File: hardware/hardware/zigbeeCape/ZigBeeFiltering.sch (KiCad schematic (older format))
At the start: 13 parts

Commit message: Finished Zigbee circuitry
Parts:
- added AE?: Antenna, symbol Device:Antenna
- added C? (x2): 1.1pF, symbol Device:C
- added C? (x2): 12pF, symbol Device:C
- added C?: 1pF, symbol Device:C
- added C? (x3): DNM, symbol Device:C
- added C?: 100pF, symbol Device:C
- added C?: 5.6pF, symbol Device:C
- added L?: 15nH, symbol Device:L
- added L? (x2): 2.4nH, symbol Device:L
- added L? (x2): 2nH, symbol Device:L
- added L?: 3.3nH, symbol Device:L
- added L?: DNM, symbol Device:L
- added R? (x2): DNM/0?, symbol Device:R
- added U?: 2.4GHz_Filter, symbol Zigbee:2.4GHz_Filter
- added U?: SMA_Antenna, symbol Zigbee:SMA_Antenna
- C? (x2): value C -> 3pF
- C? (x2): value C -> 100pF
- C?: value C -> 2.7pF
- C?: value C -> 5.6pF
- C?: value C -> 1.2pF
- L? (x2): value L -> 3.9nH
- L? (x2): value L -> 10nH
- L?: value L -> 7.5nH
- L?: value L -> 22nH
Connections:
- net GND: now also C?.1, C?.2, C?.2, C?.2, C?.2, L?.2, U?.2, U?.2 (GND), U?.3, U?.4, U?.4 (GND), U?.5
- net RX_TX: now also C?.2, L?.1
- net SUB-1_GHz_RF_N renamed SUB-1_GHZ_RF_N
- net SUB-1_GHz_RF_Out: no longer names the net of C?.2
- net SUB-1_GHz_RF_Out: now also R?.2
- net SUB-1_GHz_RF_P renamed SUB-1_GHZ_RF_P
- new net: C?.2, L?.1, L?.2
- new net: C?.1, L?.1, L?.2
- new net: C?.1, C?.1, L?.2
- new net: C?.2, U?.1 (IN)
- new net: R?.1, U?.3 (OUT)
- new net: C?.1, U?.1 (INPUT)
- new net: C?.2, C?.2, R?.1, R?.2
- new net: C?.1, L?.1
- new net: C?.1, C?.1, L?.1, L?.2
- new net: AE?.1 (A), C?.2
- new net 2_4_GHZ_RF_N: C?.1, L?.1, L?.2
- new net 2_4_GHZ_RF_P: C?.1, L?.1, L?.2
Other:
- note added: "Above 3 caps are changed due to lack of FL3"
- note added: "Check if caps are needed"
- note added: "Do we need to choose?"
- note added: "Last 2 caps and inductor are for Antenna matching\n"
- note added: "Should we include P11 and P12?"
- note added: "Will this simplify debugging?"
- moved on the sheet: C?, L?

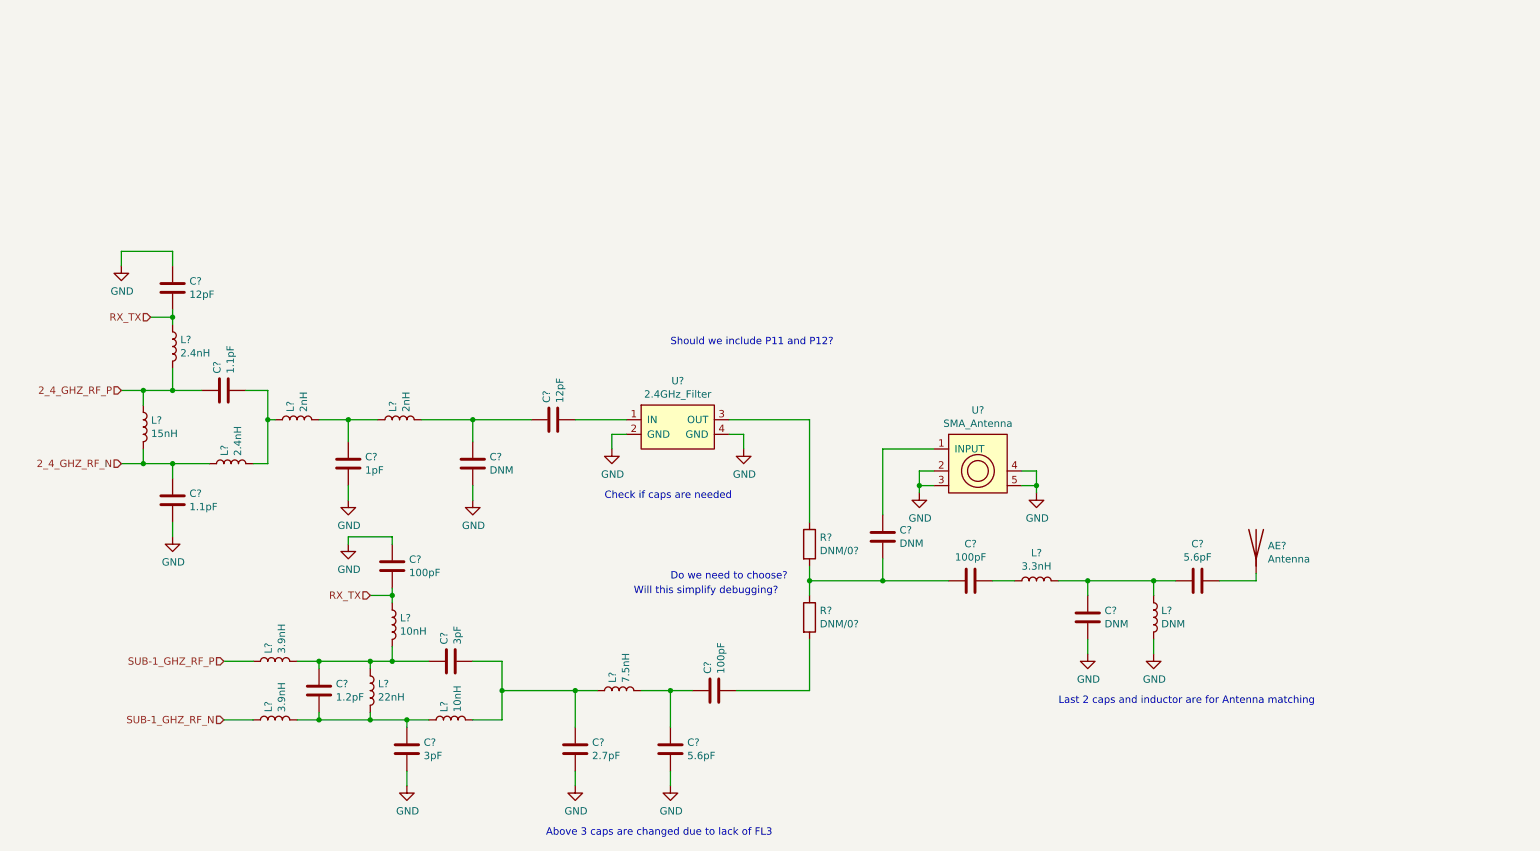
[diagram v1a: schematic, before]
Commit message: Assigned Pin types, cleaned stuff up, Fixed most errors from the DRC (questions on the last few)
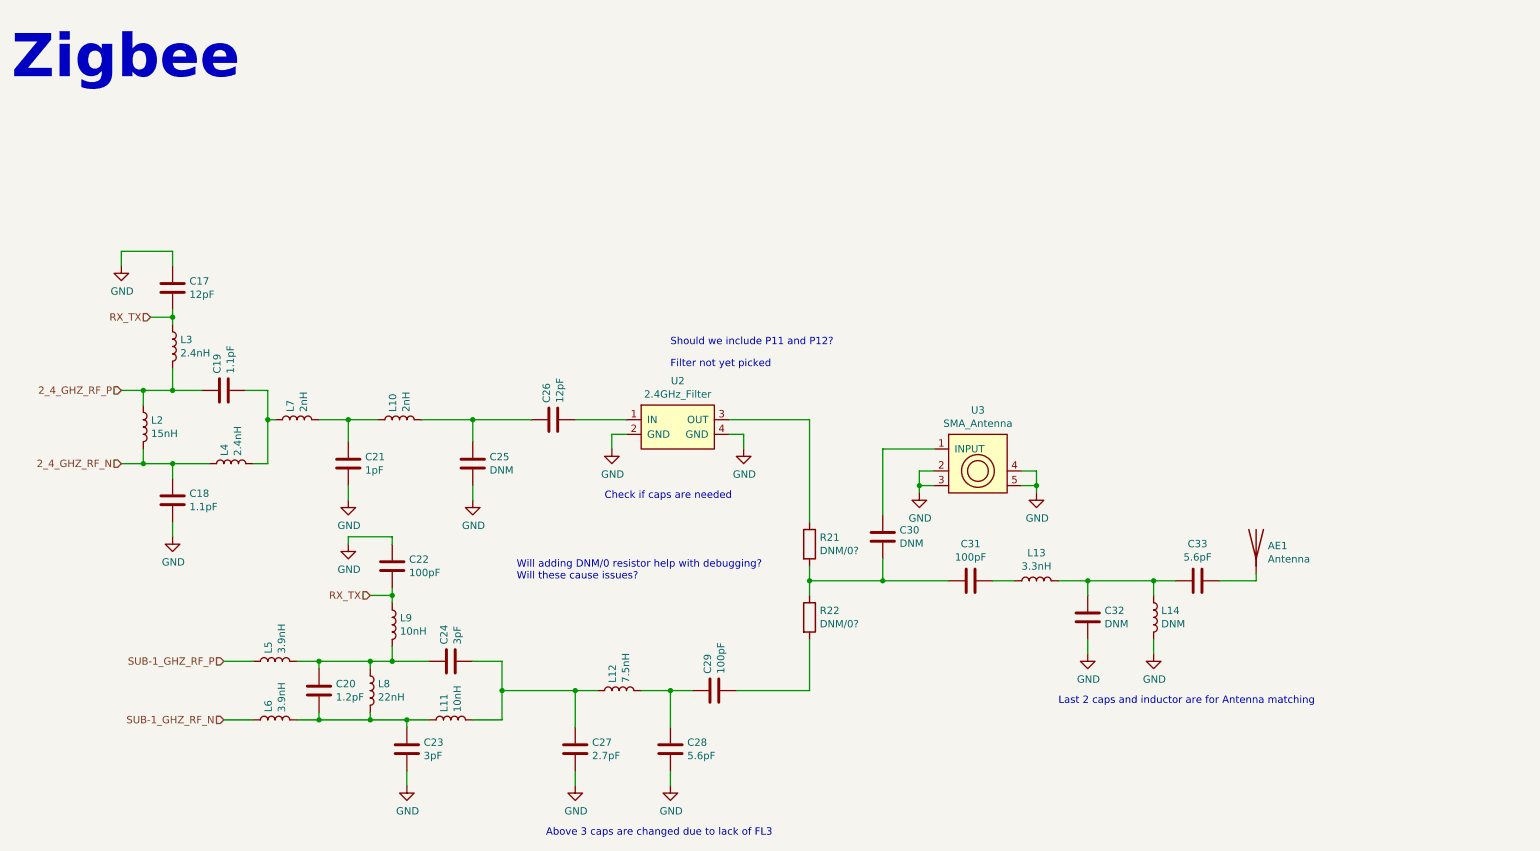
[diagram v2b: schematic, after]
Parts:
- gave numbers to parts that had none: 35
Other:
- note added: "Filter not yet picked"
- note added: "Will adding DNM/0 resistor help with debugging?\nWill these cause issues?"
- note added: "Zigbee"
- note removed: "Do we need to choose?"
- note removed: "Will this simplify debugging?"

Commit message: Added FL3 2.4ghz filter DPX252690DT-5032B1
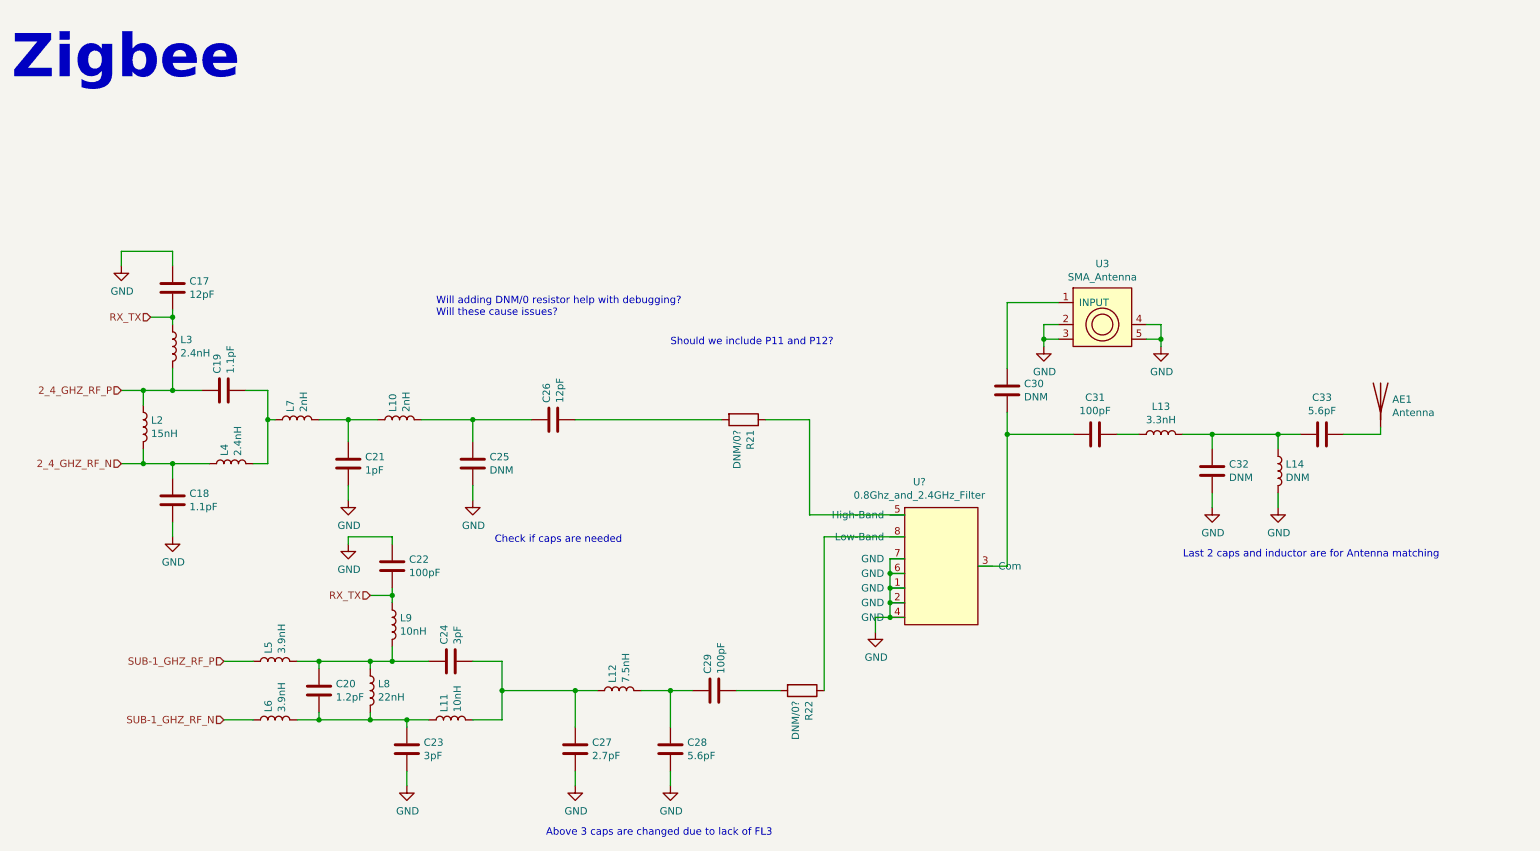
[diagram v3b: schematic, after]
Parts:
- removed U2: 2.4GHz_Filter, symbol Zigbee:2.4GHz_Filter
- added U?: 0.8Ghz_and_2.4GHz_Filter, symbol Zigbee:0.8Ghz_and_2.4GHz_Filter
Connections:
- net GND: now also U?.1 (GND), U?.2 (GND), U?.4 (GND), U?.6 (GND), U?.7 (GND)
- net at C26.2: now also R21.2
- net at R21.1: now also U?.5 (High-Band)
- net at C30.2, C31.2: now also U?.3 (Com); no longer R21.2, R22.1
- new net: R22.1, U?.8 (Low-Band)
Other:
- note removed: "Filter not yet picked"
- moved on the sheet: AE1, C30, C31, C32, C33, L13, L14, R21, R22, U3

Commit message: Fixed a few little things
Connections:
- net GND: no longer U?.1 (GND), U?.6 (GND)
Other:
- note added: "Check FL3 replacement and change parts acorrdingly"
- note added: "Remove R21 and R22"
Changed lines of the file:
@@
 	6750 4250 6650 4250
-Wire Wire Line
-	6650 4250 6650 4350
-Wire Wire Line
-	6650 4350 6750 4350
-Wire Wire Line
-	6750 4450 6650 4450
 Wire Wire Line
 	6650 4550 6750 4550
 Wire Wire Line
 	6750 4650 6650 4650
-Wire Wire Line
-	6650 4350 6650 4450
-Connection ~ 6650 4350
-Connection ~ 6650 4450
-Wire Wire Line
-	6650 4450 6650 4550
 Connection ~ 6650 4550
 Wire Wire Line
@@
 	7450 4300 7250 4300
 Connection ~ 7450 3400
+Text Notes 5450 4300 0    39   ~ 0
+Remove R21 and R22
+Text Notes 5950 5700 0    39   ~ 0
+Check FL3 replacement and change parts acorrdingly
+Wire Wire Line
+	6650 4250 6650 4550
 $EndSCHEMATC

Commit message: Fixing Git issue
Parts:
- removed R21, R22: DNM/0?, symbol Device:R
- C27: value 2.7pF -> DNM
- C28: value 5.6pF -> 3.6pF
- L12: value 7.5nH -> 9.1nH
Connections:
- net GND: now also U?.1 (GND), U?.6 (GND)
- net at C26.2: now also U?.5 (High-Band)
- net at C29.2: now also U?.8 (Low-Band)
- net at C30.2, C31.2: no longer U?.3 (Com)
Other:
- note removed: "Above 3 caps are changed due to lack of FL3"
- note removed: "Check FL3 replacement and change parts acorrdingly"
- note removed: "Check if caps are needed"
- note removed: "Remove R21 and R22"
- note removed: "Will adding DNM/0 resistor help with debugging?\nWill these cause issues?"
- moved on the sheet: AE1, C17, C18, C19, C20, C21, C22, C23, C24, C25, C26, C27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

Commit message: Started BOM
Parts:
- gave numbers to parts that had none: 1
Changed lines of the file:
@@
 Zigbee
 $Comp
-L Zigbee:0.8Ghz_and_2.4GHz_Filter U?
+L Zigbee:0.8Ghz_and_2.4GHz_Filter U2
 U 1 1 6091DA9B
 P 6300 4150
-F 0 "U?" H 6150 4625 50  0000 C CNN
+F 0 "U2" H 6150 4625 50  0000 C CNN
 F 1 "0.8Ghz_and_2.4GHz_Filter" H 6150 4534 50  0000 C CNN
 F 2 "" H 6200 4150 50  0001 C CNN

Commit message: Added excell file to document deviations from CC1352R1 footprint size. Started assigning Footprints for Zigbee cape
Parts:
- AE1: footprint (none) -> Connector_Coaxial:SMA_Amphenol_132134-16_Vertical
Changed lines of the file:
@@
 F 0 "AE1" H 9780 3989 50  0000 L CNN
 F 1 "Antenna" H 9780 3898 50  0000 L CNN
-F 2 "" H 9700 4000 50  0001 C CNN
+F 2 "Connector_Coaxial:SMA_Amphenol_132134-16_Vertical" H 9700 4000 50  0001 C CNN
 F 3 "~" H 9700 4000 50  0001 C CNN
 	1    9700 4000

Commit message: Added items to BOM. Added footprints to GIT. Finished Capacitor footprint association. Finished LED footprint association.
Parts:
- C17, C18, C19, C20, C21, C22, C23, C24, C25, C26, C27, C28, C29, C30, C31, C32, C33: footprint (none) -> Capacitor_SMD:C_0603_1608Metric_Pad1.08x0.95mm_HandSolder
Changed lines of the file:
@@
 F 0 "C24" H 3515 4946 50  0000 L CNN
 F 1 "3pF" H 3515 4855 50  0000 L CNN
-F 2 "" H 3438 4750 50  0001 C CNN
+F 2 "Capacitor_SMD:C_0603_1608Metric_Pad1.08x0.95mm_HandSolder" H 3438 4750 50  0001 C CNN
 F 3 "~" H 3400 4900 50  0001 C CNN
 	1    3400 4900
@@
 F 0 "C22" H 3115 4296 50  0000 L CNN
 F 1 "100pF" H 3115 4205 50  0000 L CNN
-F 2 "" H 3038 4100 50  0001 C CNN
+F 2 "Capacitor_SMD:C_0603_1608Metric_Pad1.08x0.95mm_HandSolder" H 3038 4100 50  0001 C CNN
 F 3 "~" H 3000 4250 50  0001 C CNN
 	1    3000 4250
@@
 F 0 "C27" H 4365 5546 50  0000 L CNN
 F 1 "DNM" H 4365 5455 50  0000 L CNN
-F 2 "" H 4288 5350 50  0001 C CNN
+F 2 "Capacitor_SMD:C_0603_1608Metric_Pad1.08x0.95mm_HandSolder" H 4288 5350 50  0001 C CNN
 F 3 "~" H 4250 5500 50  0001 C CNN
 	1    4250 5500
@@
 F 0 "C28" H 5015 5546 50  0000 L CNN
 F 1 "3.6pF" H 5015 5455 50  0000 L CNN
-F 2 "" H 4938 5350 50  0001 C CNN
+F 2 "Capacitor_SMD:C_0603_1608Metric_Pad1.08x0.95mm_HandSolder" H 4938 5350 50  0001 C CNN
 F 3 "~" H 4900 5500 50  0001 C CNN
 	1    4900 5500
@@
 F 0 "C29" H 5315 5146 50  0000 L CNN
 F 1 "100pF" H 5315 5055 50  0000 L CNN
-F 2 "" H 5238 4950 50  0001 C CNN
+F 2 "Capacitor_SMD:C_0603_1608Metric_Pad1.08x0.95mm_HandSolder" H 5238 4950 50  0001 C CNN
 F 3 "~" H 5200 5100 50  0001 C CNN
 	1    5200 5100
@@
 F 0 "C23" H 3215 5546 50  0000 L CNN
 F 1 "3pF" H 3215 5455 50  0000 L CNN
-F 2 "" H 3138 5350 50  0001 C CNN
+F 2 "Capacitor_SMD:C_0603_1608Metric_Pad1.08x0.95mm_HandSolder" H 3138 5350 50  0001 C CNN
 F 3 "~" H 3100 5500 50  0001 C CNN
 	1    3100 5500
@@
 F 0 "C20" H 2615 5146 50  0000 L CNN
 F 1 "1.2pF" H 2615 5055 50  0000 L CNN
-F 2 "" H 2538 4950 50  0001 C CNN
+F 2 "Capacitor_SMD:C_0603_1608Metric_Pad1.08x0.95mm_HandSolder" H 2538 4950 50  0001 C CNN
 F 3 "~" H 2500 5100 50  0001 C CNN
 	1    2500 5100
@@
 F 0 "C19" H 2965 3046 50  0000 L CNN
 F 1 "1.1pF" H 2965 2955 50  0000 L CNN
-F 2 "" H 2888 2850 50  0001 C CNN
+F 2 "Capacitor_SMD:C_0603_1608Metric_Pad1.08x0.95mm_HandSolder" H 2888 2850 50  0001 C CNN
 F 3 "~" H 2850 3000 50  0001 C CNN
 	1    2850 3000
@@
 F 0 "C26" H 5215 3246 50  0000 L CNN
 F 1 "12pF" H 5215 3155 50  0000 L CNN
-F 2 "" H 5138 3050 50  0001 C CNN
+F 2 "Capacitor_SMD:C_0603_1608Metric_Pad1.08x0.95mm_HandSolder" H 5138 3050 50  0001 C CNN
 F 3 "~" H 5100 3200 50  0001 C CNN
 	1    5100 3200
@@
 F 0 "C25" H 4665 3546 50  0000 L CNN
 F 1 "DNM" H 4665 3455 50  0000 L CNN
-F 2 "" H 4588 3350 50  0001 C CNN
+F 2 "Capacitor_SMD:C_0603_1608Metric_Pad1.08x0.95mm_HandSolder" H 4588 3350 50  0001 C CNN
 F 3 "~" H 4550 3500 50  0001 C CNN
 	1    4550 3500
@@
 F 0 "C21" H 3815 3546 50  0000 L CNN
 F 1 "1pF" H 3815 3455 50  0000 L CNN
-F 2 "" H 3738 3350 50  0001 C CNN
+F 2 "Capacitor_SMD:C_0603_1608Metric_Pad1.08x0.95mm_HandSolder" H 3738 3350 50  0001 C CNN
 F 3 "~" H 3700 3500 50  0001 C CNN
 	1    3700 3500
@@
 F 0 "C17" H 2615 2346 50  0000 L CNN
 F 1 "12pF" H 2615 2255 50  0000 L CNN
-F 2 "" H 2538 2150 50  0001 C CNN
+F 2 "Capacitor_SMD:C_0603_1608Metric_Pad1.08x0.95mm_HandSolder" H 2538 2150 50  0001 C CNN
 F 3 "~" H 2500 2300 50  0001 C CNN
 	1    2500 2300
@@
 F 0 "C18" H 2615 3796 50  0000 L CNN
 F 1 "1.1pF" H 2615 3705 50  0000 L CNN
-F 2 "" H 2538 3600 50  0001 C CNN
+F 2 "Capacitor_SMD:C_0603_1608Metric_Pad1.08x0.95mm_HandSolder" H 2538 3600 50  0001 C CNN
 F 3 "~" H 2500 3750 50  0001 C CNN
 	1    2500 3750
@@
 F 0 "C31" V 7498 4250 50  0000 C CNN
 F 1 "100pF" V 7589 4250 50  0000 C CNN
-F 2 "" H 7788 4100 50  0001 C CNN
+F 2 "Capacitor_SMD:C_0603_1608Metric_Pad1.08x0.95mm_HandSolder" H 7788 4100 50  0001 C CNN
 F 3 "~" H 7750 4250 50  0001 C CNN
 	1    7750 4250
@@
 F 0 "C30" H 7265 3996 50  0000 L CNN
 F 1 "DNM" H 7265 3905 50  0000 L CNN
-F 2 "" H 7188 3800 50  0001 C CNN
+F 2 "Capacitor_SMD:C_0603_1608Metric_Pad1.08x0.95mm_HandSolder" H 7188 3800 50  0001 C CNN
 F 3 "~" H 7150 3950 50  0001 C CNN
 	1    7150 3950
@@
 F 0 "C32" H 8665 4546 50  0000 L CNN
 F 1 "DNM" H 8665 4455 50  0000 L CNN
-F 2 "" H 8588 4350 50  0001 C CNN
+F 2 "Capacitor_SMD:C_0603_1608Metric_Pad1.08x0.95mm_HandSolder" H 8588 4350 50  0001 C CNN
 F 3 "~" H 8550 4500 50  0001 C CNN
 	1    8550 4500
@@
 F 0 "C33" V 9552 4250 50  0000 C CNN
 F 1 "5.6pF" V 9461 4250 50  0000 C CNN
-F 2 "" H 9338 4100 50  0001 C CNN
+F 2 "Capacitor_SMD:C_0603_1608Metric_Pad1.08x0.95mm_HandSolder" H 9338 4100 50  0001 C CNN
 F 3 "~" H 9300 4250 50  0001 C CNN
 	1    9300 4250
